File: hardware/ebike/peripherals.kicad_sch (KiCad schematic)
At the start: 0 parts

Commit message: wired most of peripherals
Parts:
- added J3: Conn_01x04_Pin, symbol Connector:Conn_01x04_Pin
- added J4: Conn_01x03_Pin, symbol Connector:Conn_01x03_Pin
- added LS1: PS1240P02BT, PS1240P02BT:XDCR_PS1240P02BT, symbol Buzzer:PS1240P02BT
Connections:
- new net +5V: J3.1 (Pin_1)
- new net BuzzerPWM: LS1.1
- new net DisplayRX: J3.2 (Pin_2)
- new net DisplayTX: J3.3 (Pin_3)
- new net GND: J3.4 (Pin_4), J4.3 (Pin_3), LS1.2
- new net ThrottleADC: J4.2 (Pin_2)
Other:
- note added: "Buzzer"
- note added: "Display header pins"
- note added: "TODO: Link throttle ADC to STM and Buzzer to GPIO, and determine power rail for throttle. Also need to find a throttle"
- note added: "Throttle Connection"

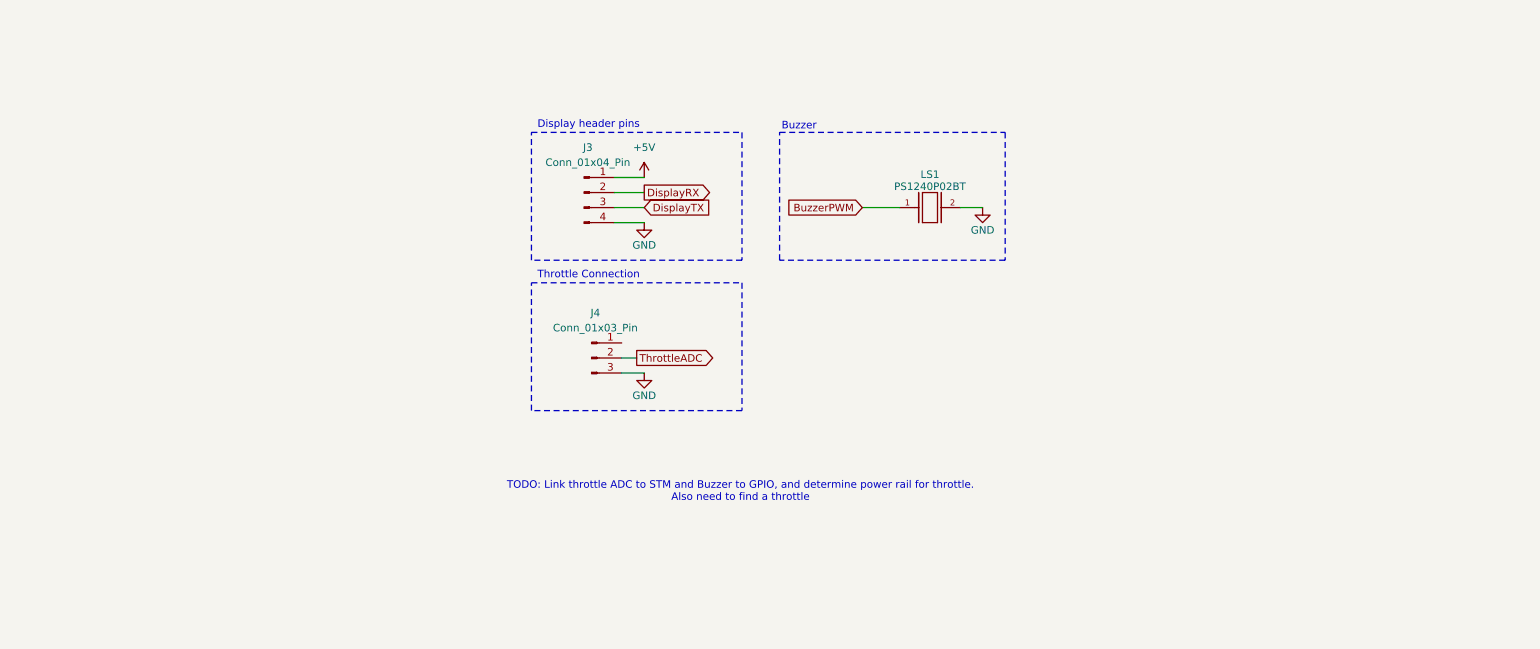
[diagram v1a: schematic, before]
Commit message: Added all peripherals and started modifying power circuitry
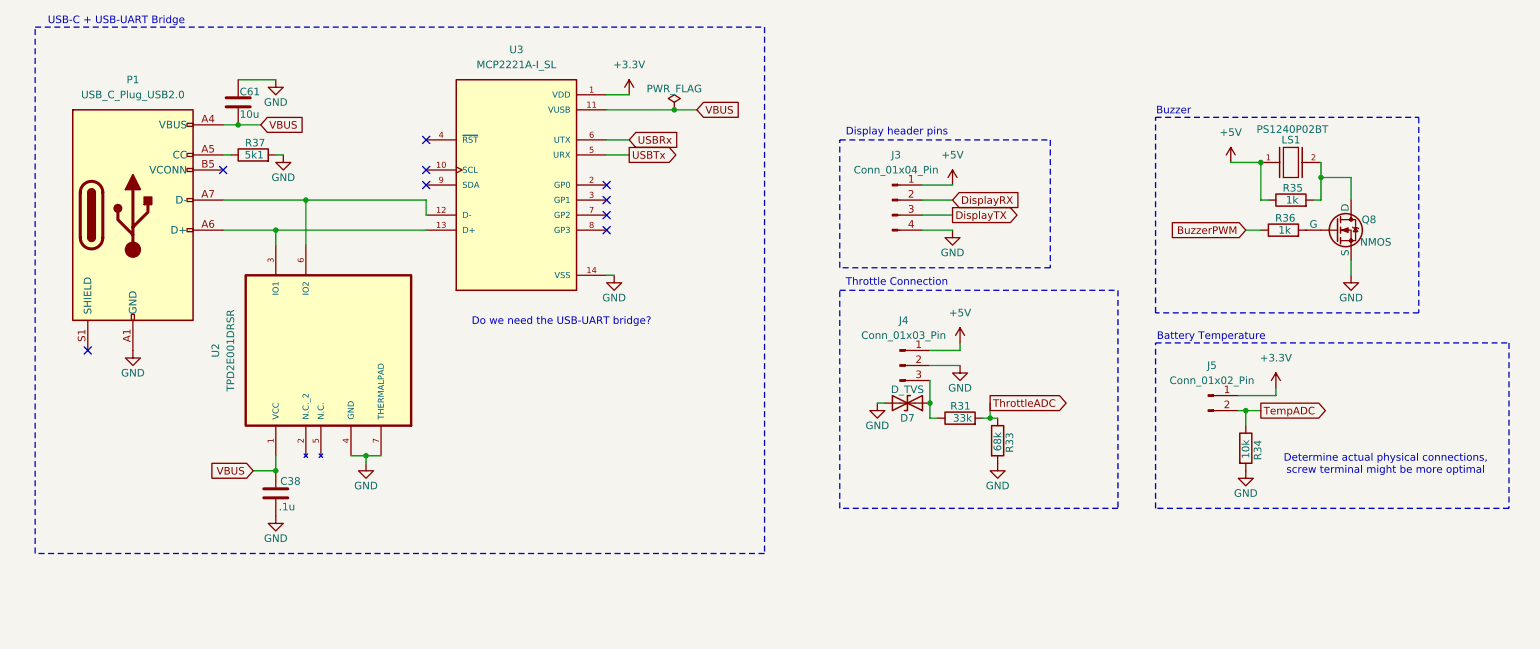
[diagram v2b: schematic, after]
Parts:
- added C38: .1u, symbol Device:C
- added C61: 10u, symbol Device:C
- added D7: D_TVS, symbol Device:D_TVS
- added J5: Conn_01x02_Pin, symbol Connector:Conn_01x02_Pin
- added P1: USB_C_Plug_USB2.0, symbol Connector:USB_C_Plug_USB2.0
- added Q8: NMOS, symbol Simulation_SPICE:NMOS
- added R31: 33k, symbol Device:R
- added R33: 68k, symbol Device:R
- added R34: 10k, symbol Device:R
- added R35, R36: 1k, symbol Device:R
- added R37: 5k1, symbol Device:R
- added U2: TPD2E001DRSR, TPD2E001DRSR:SON95P315X315X80-7N, symbol TI_ESD:TPD2E001DRSR
- added U3: MCP2221A-I_SL, MCP2221A-I_SL:SOIC127P600X175-14N, symbol Bridge:MCP2221A-I_SL
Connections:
- net +5V: now also J4.1 (Pin_1), LS1.1, R35.1
- net BuzzerPWM: now also R36.1; no longer LS1.1
- net GND: now also J4.2 (Pin_2), C38.2, C61.2, D7.2 (A2), P1.A1 (GND), P1.A12 (GND), P1.B1 (GND), P1.B12 (GND), Q8.3 (S), R33.2, R34.2, R37.2, U2.4 (GND), U2.7 (THERMALPAD), U3.14 (VSS); no longer J4.3 (Pin_3), LS1.2
- net ThrottleADC: now also R31.2, R33.1; no longer J4.2 (Pin_2)
- new net: LS1.2, Q8.1 (D), R35.2
- new net: P1.A7 (D-), U2.6 (IO2), U3.12 (D-)
- new net: P1.A6 (D+), U2.3 (IO1), U3.13 (D+)
- new net: D7.1 (A1), J4.3 (Pin_3), R31.1
- new net: Q8.2 (G), R36.2
- new net: P1.A5 (CC), R37.1
- new net +3.3V: J5.1 (Pin_1), U3.1 (VDD)
- new net TempADC: J5.2 (Pin_2), R34.1
- new net USBRx: U3.6 (UTX)
- new net USBTx: U3.5 (URX)
- new net VBUS: C38.1, C61.1, P1.A4 (VBUS), P1.A9 (VBUS), P1.B4 (VBUS), P1.B9 (VBUS), U2.1 (VCC), U3.11 (VUSB)
- no-connect marks 0 -> 9
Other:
- note added: "Battery Temperature"
- note added: "Determine actual physical connections, screw terminal might be more optimal"
- note added: "Do we need the USB-UART bridge?"
- note added: "USB-C + USB-UART Bridge"
- note removed: "TODO: Link throttle ADC to STM and Buzzer to GPIO, and determine power rail for throttle. Also need to find a throttle"
- moved on the sheet: J3, J4, LS1

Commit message: schematic ready for first review
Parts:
- added D10, D9: LED, symbol Device:LED
- added R38, R39: 1k, symbol Device:R
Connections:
- net GND: now also D10.1 (K), D9.1 (K)
- new net: D10.2 (A), R39.2
- new net: D9.2 (A), R38.2
- new net LED1: R38.1
- new net LED2: R39.1
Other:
- note added: "Programmable Status LEDs"
- note removed: "Do we need the USB-UART bridge?"

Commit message: finished annoation for schematic
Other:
- note added: "Determine actual physical connections, screw terminal might be more optimal for thermosistor"
- note removed: "Determine actual physical connections, screw terminal might be more optimal"
- moved on the sheet: D7, J4, R31, R33

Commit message: minor fixes
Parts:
- removed D7: D_TVS, symbol Device:D_TVS
- removed Q8: NMOS, symbol Simulation_SPICE:NMOS
- removed R35, R36: 1k, symbol Device:R
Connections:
- net +5V: no longer LS1.1
- net BuzzerPWM: now also LS1.1
- net GND: now also LS1.2
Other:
- note added: "Change USBC, shouldn't be plug needs to be receptacle or sum"
- note added: "Double check this, if antenna blows up, change it"
- moved on the sheet: LS1

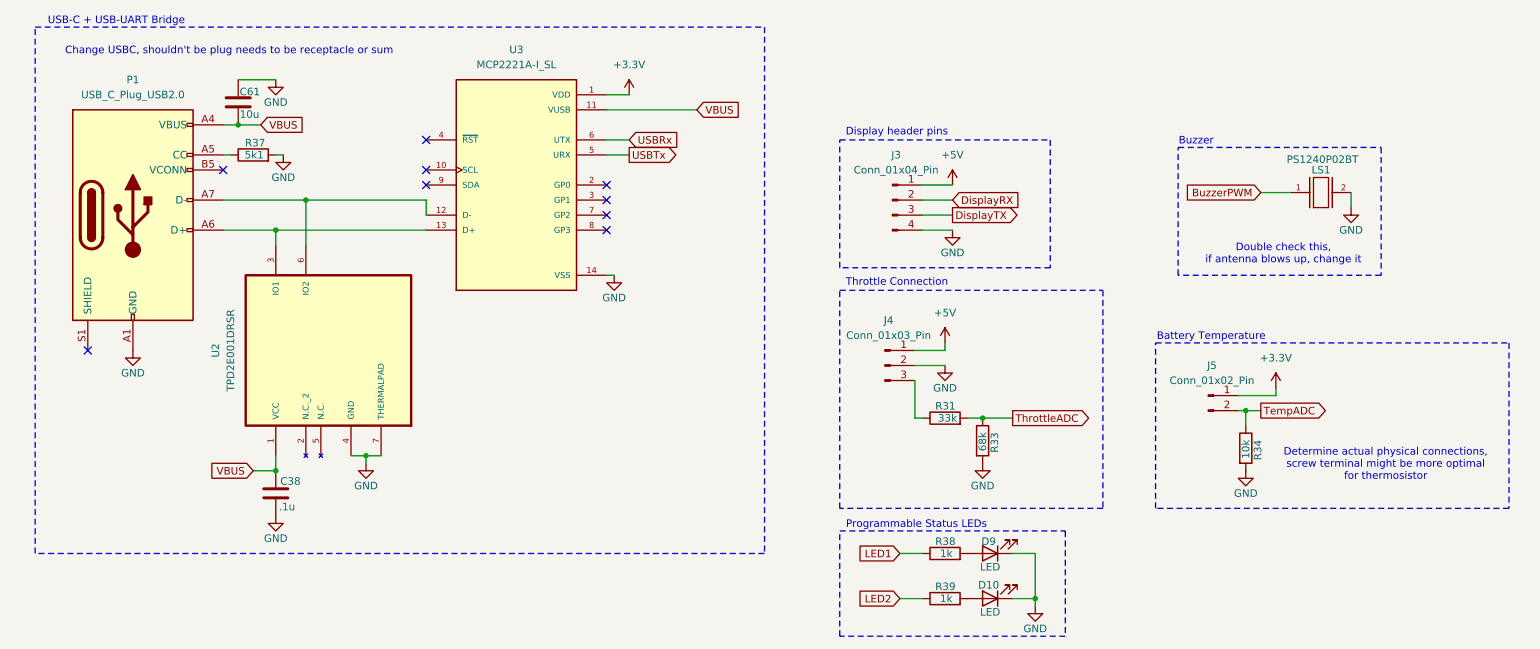
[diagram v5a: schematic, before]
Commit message: started working on footprint assignment
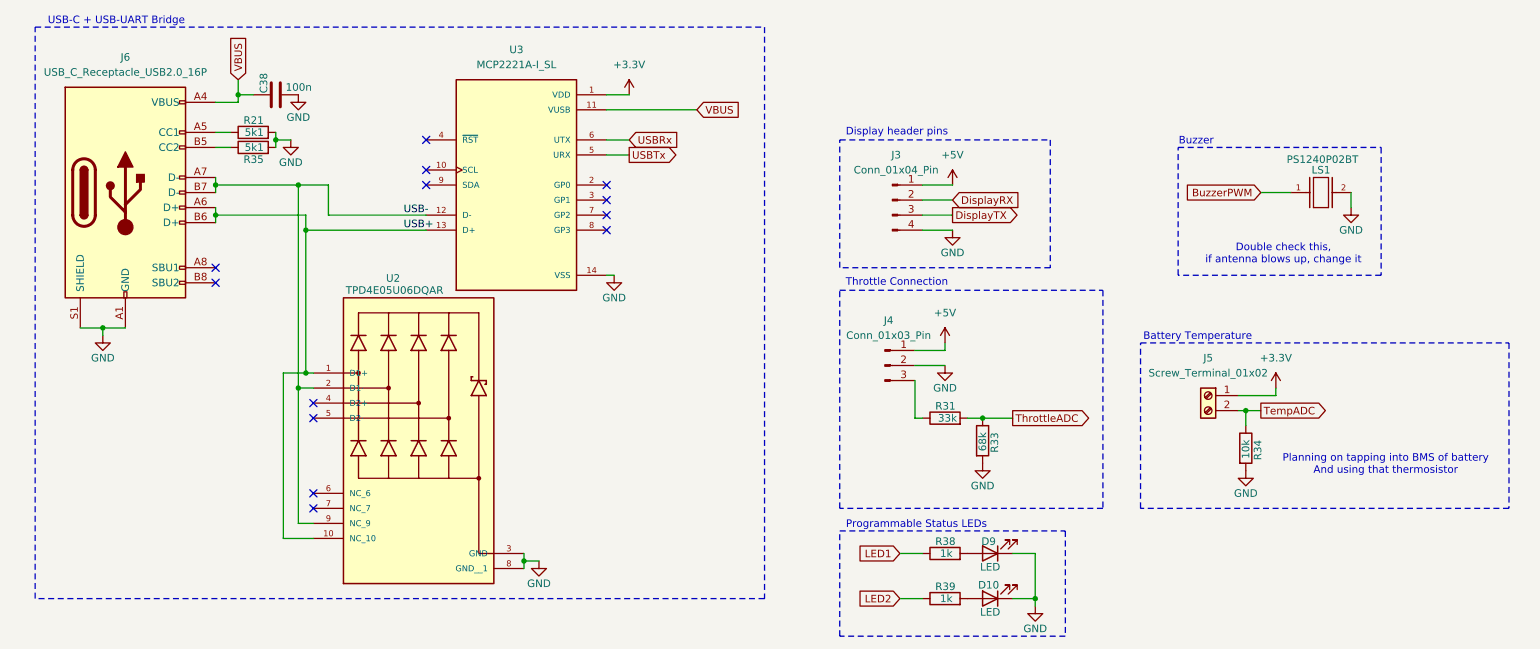
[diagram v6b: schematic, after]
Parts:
- removed C61: 10u, symbol Device:C
- removed J5: Conn_01x02_Pin, symbol Connector:Conn_01x02_Pin
- removed P1: USB_C_Plug_USB2.0, symbol Connector:USB_C_Plug_USB2.0
- removed R37: 5k1, symbol Device:R
- removed U2: TPD2E001DRSR, TPD2E001DRSR:SON95P315X315X80-7N, symbol TI_ESD:TPD2E001DRSR
- added J5: Screw_Terminal_01x02, symbol Connector:Screw_Terminal_01x02
- added J6: USB_C_Receptacle_USB2.0_16P, symbol Connector:USB_C_Receptacle_USB2.0_16P
- added R21, R35: 5k1, symbol Device:R
- added U2: TPD4E05U06DQAR, TPD4E05U06DQAR:IC_TPD4E05U06DQAR, symbol ESD:TPD4E05U06DQAR
- C38: value .1u -> 100n
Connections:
- net +3.3V: now also J5.1 (Pin_1)
- net GND: now also J6.A1 (GND), J6.A12 (GND), J6.B1 (GND), J6.B12 (GND), J6.S1 (SHIELD), R21.2, R35.2, U2.3 (GND), U2.8 (GND__1)
- net TempADC: now also J5.2 (Pin_2)
- net VBUS: now also J6.A4 (VBUS), J6.A9 (VBUS), J6.B4 (VBUS), J6.B9 (VBUS)
- net USB-: now reaches U3.12 (D-)
- net USB-: now also J6.A7 (D-), J6.B7 (D-), U2.2 (D1-), U2.9 (NC_9)
- net USB+: now reaches U3.13 (D+)
- net USB+: now also J6.A6 (D+), J6.B6 (D+), U2.1 (D1+), U2.10 (NC_10)
- new net: J6.A5 (CC1), R21.1
- new net: J6.B5 (CC2), R35.1
- no-connect marks 9 -> 13
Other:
- note added: "Planning on tapping into BMS of battery And using that thermosistor"
- note removed: "Change USBC, shouldn't be plug needs to be receptacle or sum"
- note removed: "Determine actual physical connections, screw terminal might be more optimal for thermosistor"
